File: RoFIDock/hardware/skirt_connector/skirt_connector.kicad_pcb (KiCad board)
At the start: 2 copper layers, 25.5 x 25.5 mm, 17 parts, among them J1 Cable, J10 SENSE_1, J11 SENSE_2, J12 48V_B, J13 48V_2, J14 GND_B, J15 GND_2, J16 RX_B, J17 TX_2, J2 48V_A, J3 48V_1, J4 GND_A, J5 GND_1, J6 RX_A, J7 TX_1, J8 SENSE_A, J9 SENSE_B

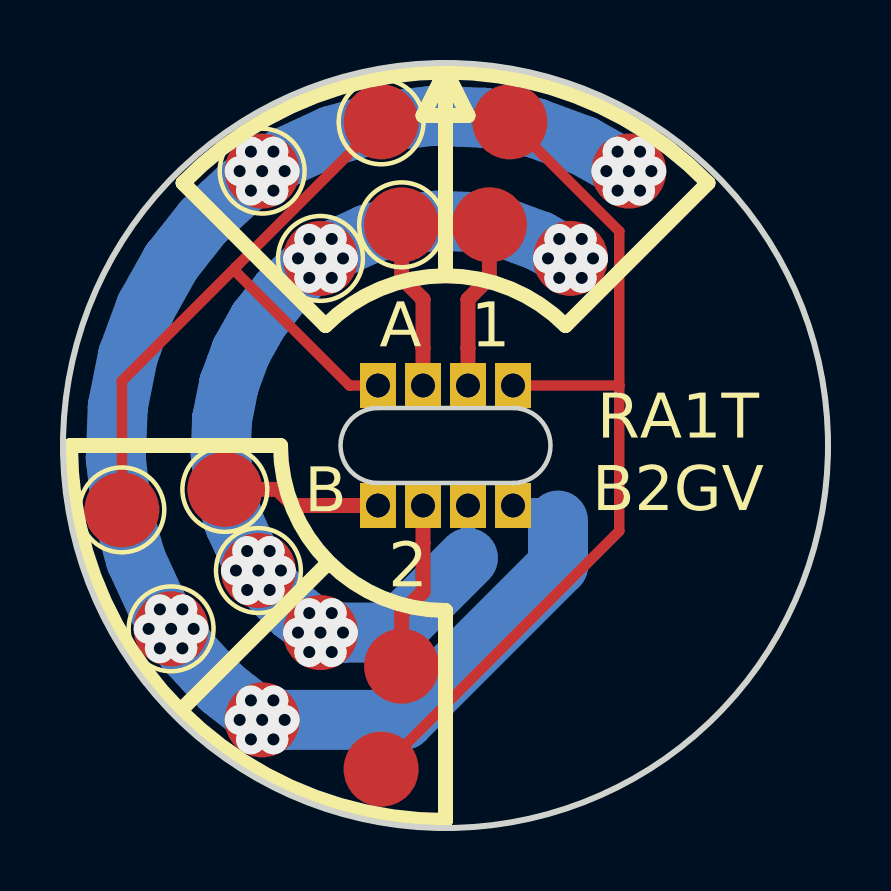
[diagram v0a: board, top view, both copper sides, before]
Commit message: dock: Update skirt connector dimensions
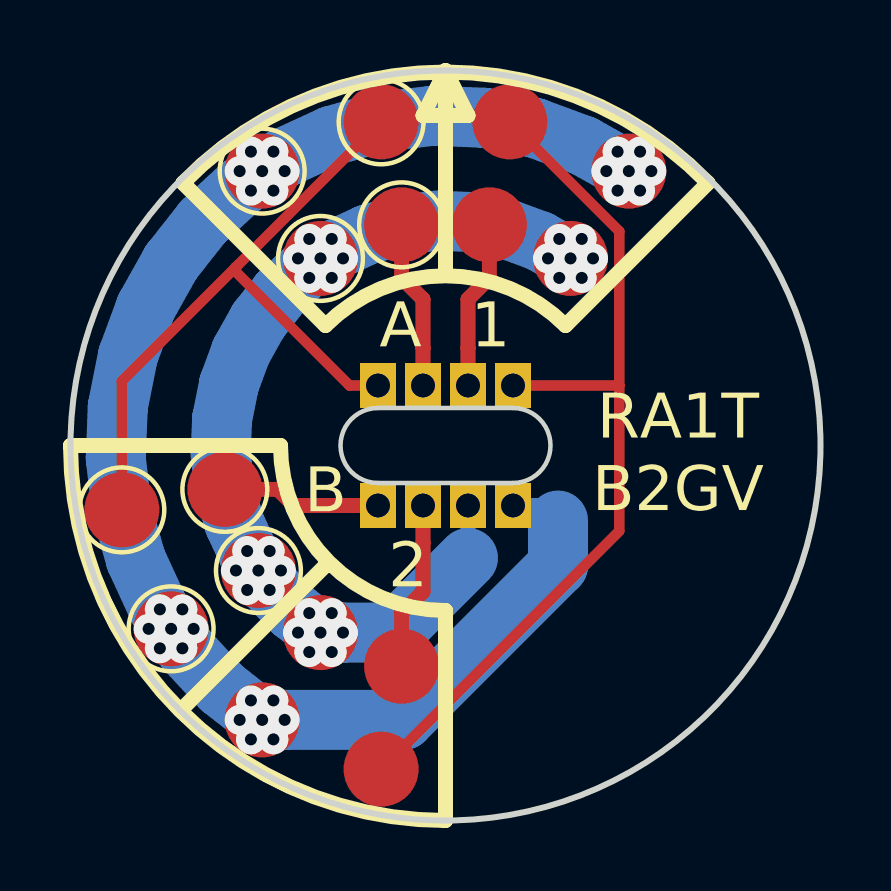
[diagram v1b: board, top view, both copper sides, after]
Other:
- board size 25.5 x 25.5 mm -> 25 x 25 mm
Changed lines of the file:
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@@
   )
   (setup
-    (last_trace_width 1)
+    (last_trace_width 0.25)
     (user_trace_width 0.35)
     (user_trace_width 0.5)
@@
     (effects (font (size 1.5 1.5) (thickness 0.3)))
   )
-  (gr_circle (center 150 100) (end 162.750035 100) (layer Edge.Cuts) (width 0.2))
+  (gr_circle (center 150 100) (end 162.5 100) (layer Edge.Cuts) (width 0.2))
   (gr_line (start 152.039376 92.633074) (end 142.039376 92.633074) (layer Eco1.User) (width 0.2))
   (gr_line (start 142.039376 92.633074) (end 142.039376 102.633074) (layer Eco1.User) (width 0.2))
